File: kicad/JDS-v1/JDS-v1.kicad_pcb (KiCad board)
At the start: 2 copper layers, 2 parts, among them U1 74HC595

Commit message: finished diode board and initial seed board
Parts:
- added D1: 1N4148, Diode_THT:D_DO-35_SOD27_P7.62mm_Horizontal, F.Cu at (157.0, 54.2)
- added D10: 1N4148, Diode_THT:D_DO-35_SOD27_P7.62mm_Horizontal, F.Cu at (130.0, 54.0)
- added D11: 1N4148, Diode_THT:D_DO-35_SOD27_P7.62mm_Horizontal, F.Cu at (127.0, 54.0)
- added D12: 1N4148, Diode_THT:D_DO-35_SOD27_P7.62mm_Horizontal, F.Cu at (124.0, 54.0)
- added D13: 1N4148, Diode_THT:D_DO-35_SOD27_P7.62mm_Horizontal, F.Cu at (121.0, 54.0)
- added D14: 1N4148, Diode_THT:D_DO-35_SOD27_P7.62mm_Horizontal, F.Cu at (118.0, 54.0)
- added D15: 1N4148, Diode_THT:D_DO-35_SOD27_P7.62mm_Horizontal, F.Cu at (115.0, 54.0)
- added D16: 1N4148, Diode_THT:D_DO-35_SOD27_P7.62mm_Horizontal, F.Cu at (112.0, 54.0)
- added D17: 1N4148, Diode_THT:D_DO-35_SOD27_P7.62mm_Horizontal, F.Cu at (157.0, 68.0)
- added D18: 1N4148, Diode_THT:D_DO-35_SOD27_P7.62mm_Horizontal, F.Cu at (154.0, 68.0)
- added D19: 1N4148, Diode_THT:D_DO-35_SOD27_P7.62mm_Horizontal, F.Cu at (151.0, 68.0)
- added D2: 1N4148, Diode_THT:D_DO-35_SOD27_P7.62mm_Horizontal, F.Cu at (154.0, 54.2)
- added D20: 1N4148, Diode_THT:D_DO-35_SOD27_P7.62mm_Horizontal, F.Cu at (148.0, 68.0)
- added D21: 1N4148, Diode_THT:D_DO-35_SOD27_P7.62mm_Horizontal, F.Cu at (145.0, 68.0)
- added D22: 1N4148, Diode_THT:D_DO-35_SOD27_P7.62mm_Horizontal, F.Cu at (142.0, 68.0)
- added D23: 1N4148, Diode_THT:D_DO-35_SOD27_P7.62mm_Horizontal, F.Cu at (139.0, 68.0)
- added D24: 1N4148, Diode_THT:D_DO-35_SOD27_P7.62mm_Horizontal, F.Cu at (136.0, 68.0)
- added D25: 1N4148, Diode_THT:D_DO-35_SOD27_P7.62mm_Horizontal, F.Cu at (133.0, 68.0)
- added D26: 1N4148, Diode_THT:D_DO-35_SOD27_P7.62mm_Horizontal, F.Cu at (130.0, 68.0)
- added D27: 1N4148, Diode_THT:D_DO-35_SOD27_P7.62mm_Horizontal, F.Cu at (127.0, 68.0)
- added D28: 1N4148, Diode_THT:D_DO-35_SOD27_P7.62mm_Horizontal, F.Cu at (124.0, 68.0)
- added D29: 1N4148, Diode_THT:D_DO-35_SOD27_P7.62mm_Horizontal, F.Cu at (121.0, 68.0)
- added D3: 1N4148, Diode_THT:D_DO-35_SOD27_P7.62mm_Horizontal, F.Cu at (151.0, 54.2)
- added D30: 1N4148, Diode_THT:D_DO-35_SOD27_P7.62mm_Horizontal, F.Cu at (118.0, 68.0)
- added D31: 1N4148, Diode_THT:D_DO-35_SOD27_P7.62mm_Horizontal, F.Cu at (115.0, 68.0)
- added D32: 1N4148, Diode_THT:D_DO-35_SOD27_P7.62mm_Horizontal, F.Cu at (112.0, 68.0)
- added D33: 1N4148, Diode_THT:D_DO-35_SOD27_P7.62mm_Horizontal, F.Cu at (157.0, 82.2)
- added D34: 1N4148, Diode_THT:D_DO-35_SOD27_P7.62mm_Horizontal, F.Cu at (154.0, 82.2)
- added D35: 1N4148, Diode_THT:D_DO-35_SOD27_P7.62mm_Horizontal, F.Cu at (151.0, 82.2)
- added D36: 1N4148, Diode_THT:D_DO-35_SOD27_P7.62mm_Horizontal, F.Cu at (148.0, 82.2)
- added D37: 1N4148, Diode_THT:D_DO-35_SOD27_P7.62mm_Horizontal, F.Cu at (145.0, 82.2)
- added D38: 1N4148, Diode_THT:D_DO-35_SOD27_P7.62mm_Horizontal, F.Cu at (142.0, 82.2)
- added D39: 1N4148, Diode_THT:D_DO-35_SOD27_P7.62mm_Horizontal, F.Cu at (139.0, 82.2)
- added D4: 1N4148, Diode_THT:D_DO-35_SOD27_P7.62mm_Horizontal, F.Cu at (148.0, 54.2)
- added D40: 1N4148, Diode_THT:D_DO-35_SOD27_P7.62mm_Horizontal, F.Cu at (136.0, 82.2)
- added D41: 1N4148, Diode_THT:D_DO-35_SOD27_P7.62mm_Horizontal, F.Cu at (133.0, 82.0)
- added D42: 1N4148, Diode_THT:D_DO-35_SOD27_P7.62mm_Horizontal, F.Cu at (130.0, 82.0)
- added D43: 1N4148, Diode_THT:D_DO-35_SOD27_P7.62mm_Horizontal, F.Cu at (127.0, 82.0)
- added D44: 1N4148, Diode_THT:D_DO-35_SOD27_P7.62mm_Horizontal, F.Cu at (124.0, 82.0)
- added D45: 1N4148, Diode_THT:D_DO-35_SOD27_P7.62mm_Horizontal, F.Cu at (121.0, 82.0)
- added D46: 1N4148, Diode_THT:D_DO-35_SOD27_P7.62mm_Horizontal, F.Cu at (118.0, 82.0)
- added D47: 1N4148, Diode_THT:D_DO-35_SOD27_P7.62mm_Horizontal, F.Cu at (115.0, 82.0)
- added D48: 1N4148, Diode_THT:D_DO-35_SOD27_P7.62mm_Horizontal, F.Cu at (112.0, 82.0)
- added D49: 1N4148, Diode_THT:D_DO-35_SOD27_P7.62mm_Horizontal, F.Cu at (157.0, 96.0)
- added D5: 1N4148, Diode_THT:D_DO-35_SOD27_P7.62mm_Horizontal, F.Cu at (145.0, 54.2)
- added D50: 1N4148, Diode_THT:D_DO-35_SOD27_P7.62mm_Horizontal, F.Cu at (154.0, 96.0)
- added D51: 1N4148, Diode_THT:D_DO-35_SOD27_P7.62mm_Horizontal, F.Cu at (151.0, 96.0)
- added D52: 1N4148, Diode_THT:D_DO-35_SOD27_P7.62mm_Horizontal, F.Cu at (148.0, 96.0)
- added D53: 1N4148, Diode_THT:D_DO-35_SOD27_P7.62mm_Horizontal, F.Cu at (145.0, 96.0)
- added D54: 1N4148, Diode_THT:D_DO-35_SOD27_P7.62mm_Horizontal, F.Cu at (142.0, 96.0)
- added D55: 1N4148, Diode_THT:D_DO-35_SOD27_P7.62mm_Horizontal, F.Cu at (139.0, 96.0)
- added D56: 1N4148, Diode_THT:D_DO-35_SOD27_P7.62mm_Horizontal, F.Cu at (136.0, 96.0)
- added D57: 1N4148, Diode_THT:D_DO-35_SOD27_P7.62mm_Horizontal, F.Cu at (133.0, 96.0)
- added D58: 1N4148, Diode_THT:D_DO-35_SOD27_P7.62mm_Horizontal, F.Cu at (130.0, 96.0)
- added D59: 1N4148, Diode_THT:D_DO-35_SOD27_P7.62mm_Horizontal, F.Cu at (127.0, 96.0)
- added D6: 1N4148, Diode_THT:D_DO-35_SOD27_P7.62mm_Horizontal, F.Cu at (142.0, 54.2)
- added D60: 1N4148, Diode_THT:D_DO-35_SOD27_P7.62mm_Horizontal, F.Cu at (124.0, 96.0)
- added D61: 1N4148, Diode_THT:D_DO-35_SOD27_P7.62mm_Horizontal, F.Cu at (121.0, 96.0)
- added D62: 1N4148, Diode_THT:D_DO-35_SOD27_P7.62mm_Horizontal, F.Cu at (118.0, 96.0)
- added D63: 1N4148, Diode_THT:D_DO-35_SOD27_P7.62mm_Horizontal, F.Cu at (115.0, 96.0)
- added D64: 1N4148, Diode_THT:D_DO-35_SOD27_P7.62mm_Horizontal, F.Cu at (112.0, 96.0)
- added D7: 1N4148, Diode_THT:D_DO-35_SOD27_P7.62mm_Horizontal, F.Cu at (139.0, 54.2)
- added D8: 1N4148, Diode_THT:D_DO-35_SOD27_P7.62mm_Horizontal, F.Cu at (136.0, 54.2)
- added D9: 1N4148, Diode_THT:D_DO-35_SOD27_P7.62mm_Horizontal, F.Cu at (133.0, 54.0)
- added J1: toPegMatrix, Connector_PinHeader_2.54mm:PinHeader_1x08_P2.54mm_Vertical, F.Cu at (176.0, 53.0)
- added J10: mInJA, Connector_PinHeader_2.54mm:PinHeader_1x08_P2.54mm_Vertical, F.Cu at (162.0, 70.0)
- added J11: mInJB, Connector_PinHeader_2.54mm:PinHeader_1x08_P2.54mm_Vertical, F.Cu at (194.0, 72.0)
- added J2: fromPegsA, Connector_PinHeader_2.54mm:PinHeader_1x08_P2.54mm_Vertical, F.Cu at (155.0, 65.0)
- added J3: fromPegsB, Connector_PinHeader_2.54mm:PinHeader_1x08_P2.54mm_Vertical, F.Cu at (131.0, 65.0)
- added J4: fromPegsC, Connector_PinHeader_2.54mm:PinHeader_1x08_P2.54mm_Vertical, F.Cu at (154.5, 79.0)
- added J5: fromPegsD, Connector_PinHeader_2.54mm:PinHeader_1x08_P2.54mm_Vertical, F.Cu at (131.0, 79.0)
- added J6: fromPegsE, Connector_PinHeader_2.54mm:PinHeader_1x08_P2.54mm_Vertical, F.Cu at (156.0, 93.0)
- added J7: fromPegsF, Connector_PinHeader_2.54mm:PinHeader_1x08_P2.54mm_Vertical, F.Cu at (131.0, 93.0)
- added J8: fromPegsG, Connector_PinHeader_2.54mm:PinHeader_1x08_P2.54mm_Vertical, F.Cu at (155.0, 107.0)
- added J9: fromPegsH, Connector_PinHeader_2.54mm:PinHeader_1x08_P2.54mm_Vertical, F.Cu at (132.0, 107.0)
- moved A1 75.6 mm to (198.5, 54.0)
- moved U1 49.2 mm to (180.0, 55.5)
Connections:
- A1 pad 10: pm-in2 -> Net-(A1-Pad10)
- A1 pad 11: pm-in3 -> Net-(A1-Pad11)
- A1 pad 12: pm-in4 -> Net-(A1-Pad12)
- A1 pad 13: pm-in5 -> Net-(A1-Pad13)
- A1 pad 14: pm-in6 -> Net-(A1-Pad14)
- A1 pad 15: pm-in7 -> Net-(A1-Pad15)
- A1 pad 4: pm-clock -> pm-serial
- A1 pad 6: pm-serial -> pm-clock
- A1 pad 8: pm-in0 -> Net-(A1-Pad8)
- A1 pad 9: pm-in1 -> Net-(A1-Pad9)
- U1 pad 1: pm-out1 -> pm-out2
- U1 pad 15: pm-out0 -> pm-out1
- U1 pad 2: pm-out2 -> pm-out3
- U1 pad 3: pm-out3 -> pm-out4
- U1 pad 4: pm-out4 -> pm-out5
- U1 pad 5: pm-out5 -> pm-out6
- U1 pad 6: pm-out6 -> pm-out7
- U1 pad 7: pm-out7 -> pm-out8
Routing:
- net pm-in2: track 0.00 -> 64.0 mm
- net pm-in8: track 0.00 -> 59.7 mm
- net pm-in4: track 0.00 -> 55.8 mm
- net pm-in6: track 0.00 -> 53.4 mm
- net +3V3: track 0.00 -> 47.8 mm
- net pm-in1: track 0.00 -> 38.9 mm
- net pm-in7: track 0.00 -> 33.9 mm
- net pm-in3: track 0.00 -> 30.2 mm
- net pm-in5: track 0.00 -> 27.0 mm
- net GND: track 0.00 -> 15.9 mm
- net pm-out1: track 0.00 -> 14.4 mm
- net pm-enable: track 0.00 -> 11.5 mm, vias 0 -> 2
- net pm-clock: track 0.00 -> 11.4 mm, vias 0 -> 2
- net pm-serial: track 0.00 -> 11.4 mm, vias 0 -> 2
- net Net-(A1-Pad9): track 0.00 -> 4.59 mm
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- added copper zone on B.Cu, net GND

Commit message: iteration, and first print files
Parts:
- added J12: Out, NateTemp:StereoJackTRS3, F.Cu at (214.0, 64.0)
- moved J1 78.0 mm to (251.0, 74.5), turned to 270 degrees
- moved U1 72.3 mm to (248.5, 78.5), turned to 270 degrees
- moved A1 67.1 mm to (250.0, 97.0), turned to 270 degrees
- moved J11 43.2 mm to (232.0, 92.5), turned to 270 degrees
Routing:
- net toAmpR: track 0.00 -> 26.8 mm
- net toAmpL: track 0.00 -> 19.3 mm

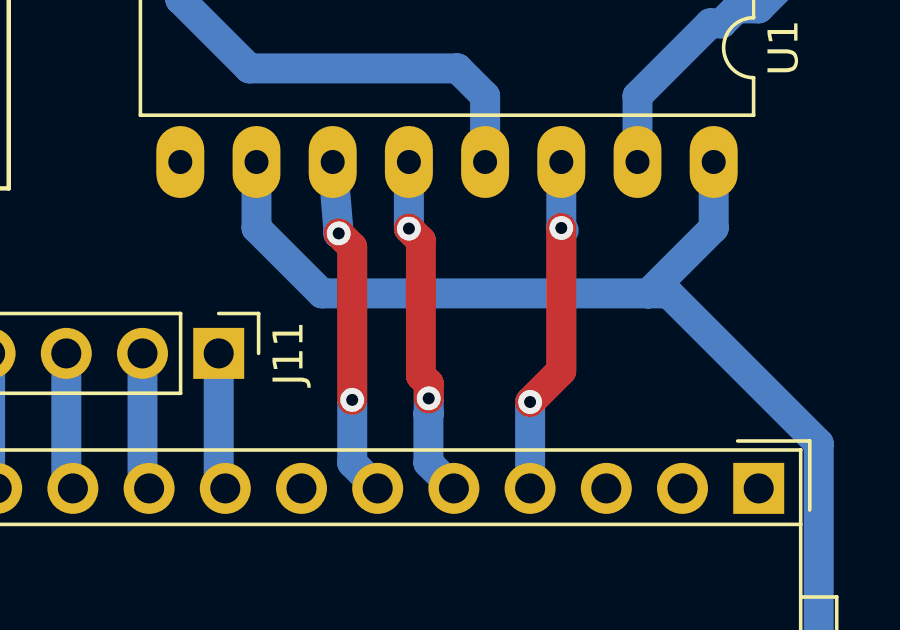
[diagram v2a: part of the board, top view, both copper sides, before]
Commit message: swapped 4 and 6 pins from seed to 595
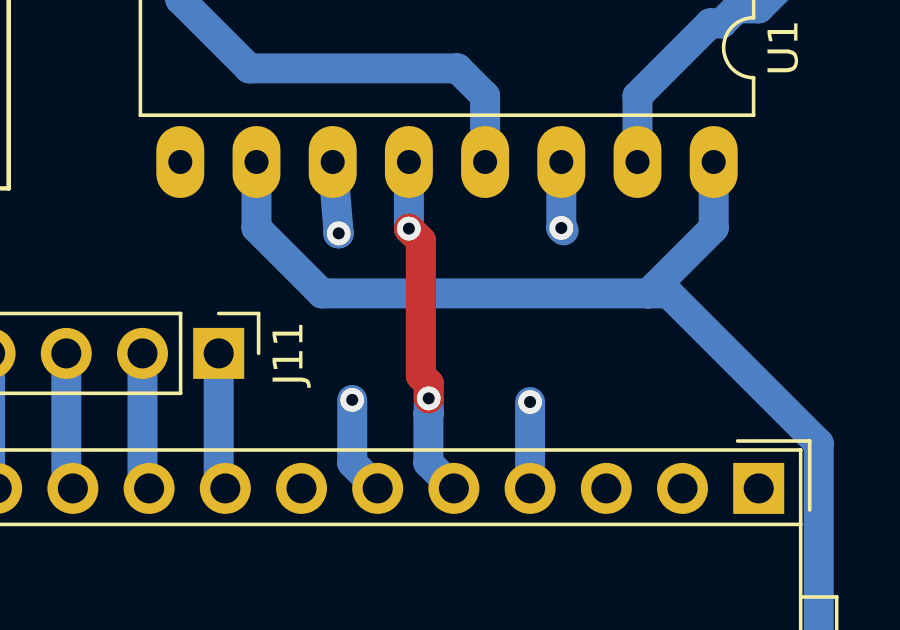
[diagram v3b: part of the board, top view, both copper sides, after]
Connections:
- A1 pad 4: pm-serial -> pm-clock
- A1 pad 6: pm-clock -> pm-serial
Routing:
- net pm-clock: track 11.4 -> 5.29 mm
- net pm-serial: track 11.4 -> 5.62 mm
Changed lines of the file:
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@@
-(kicad_pcb (version 20171130) (host pcbnew "(5.1.5-0)")
+(kicad_pcb (version 20171130) (host pcbnew "(5.0.0)")
   (general
     (thickness 1.6)
     (drawings 0)
-    (tracks 267)
+    (tracks 263)
     (zones 0)
     (modules 78)
@@
   )
   (setup
-    (last_trace_width 1)
+    (last_trace_width 0.25)
     (user_trace_width 0.5)
     (user_trace_width 1)
@@
     (zone_45_only no)
     (trace_min 0.2)
+    (segment_width 0.2)
+    (edge_width 0.05)
     (via_size 0.8)
     (via_drill 0.4)
@@
     (uvia_min_size 0.2)
     (uvia_min_drill 0.1)
-    (edge_width 0.05)
-    (segment_width 0.2)
     (pcb_text_width 0.3)
     (pcb_text_size 1.5 1.5)
@@
     (solder_mask_min_width 0.25)
     (aux_axis_origin 0 0)
-    (visible_elements FFFFFF7F)
+    (visible_elements 7FFFFFFF)
     (pcbplotparams
       (layerselection 0x010fc_ffffffff)
@@
       (net 44 "Net-(A1-Pad7)"))
     (pad 6 thru_hole circle (at 0 12.7 270) (size 1.7 1.7) (drill 1) (layers *.Cu *.Mask)
-      (net 9 pm-clock))
+      (net 4 pm-serial))
     (pad 5 thru_hole circle (at 0 10.16 270) (size 1.7 1.7) (drill 1) (layers *.Cu *.Mask)
       (net 7 pm-enable))
     (pad 4 thru_hole circle (at 0 7.62 270) (size 1.7 1.7) (drill 1) (layers *.Cu *.Mask)
-      (net 4 pm-serial))
+      (net 9 pm-clock))
     (pad 3 thru_hole circle (at 0 5.08 270) (size 1.7 1.7) (drill 1) (layers *.Cu *.Mask)
       (net 45 "Net-(A1-Pad3)"))
@@
   (segment (start 243.42 88.32) (end 243.42 88.32) (width 1) (layer B.Cu) (net 4))
   (via (at 243.42 88.32) (size 0.8) (drill 0.4) (layers F.Cu B.Cu) (net 4))
-  (segment (start 242.38 97) (end 242.38 94.12) (width 1) (layer B.Cu) (net 4))
-  (segment (start 242.38 94.12) (end 242.38 94.12) (width 1) (layer B.Cu) (net 4))
-  (via (at 242.38 94.12) (size 0.8) (drill 0.4) (layers F.Cu B.Cu) (net 4))
-  (segment (start 243.42 93.08) (end 242.38 94.12) (width 1) (layer F.Cu) (net 4))
-  (segment (start 243.42 88.32) (end 243.42 93.08) (width 1) (layer F.Cu) (net 4))
+  (segment (start 242.38 97) (end 242.38 94.12) (width 1) (layer B.Cu) (net 9))
+  (segment (start 242.38 94.12) (end 242.38 94.12) (width 1) (layer B.Cu) (net 9))
+  (via (at 242.38 94.12) (size 0.8) (drill 0.4) (layers F.Cu B.Cu) (net 9))
   (segment (start 238.3 78.46) (end 238.34 78.5) (width 1) (layer B.Cu) (net 5))
   (segment (start 238.3 74.5) (end 238.3 78.46) (width 1) (layer B.Cu) (net 5))
@@
   (segment (start 235.8 86.12) (end 236 88.5) (width 1) (layer B.Cu) (net 9))
   (segment (start 236 88.5) (end 236 88.5) (width 1) (layer B.Cu) (net 9))
-  (via (at 236 88.5) (size 0.8) (drill 0.4) (layers F.Cu B.Cu) (net 9) (status 1000000))
-  (segment (start 236.450001 96.150001) (end 236.450001 94.049999) (width 1) (layer B.Cu) (net 9))
-  (segment (start 237.3 97) (end 236.450001 96.150001) (width 1) (layer B.Cu) (net 9))
-  (segment (start 236.450001 94.049999) (end 236.450001 94.049999) (width 1) (layer B.Cu) (net 9))
-  (via (at 236.450001 94.049999) (size 0.8) (drill 0.4) (layers F.Cu B.Cu) (net 9))
-  (segment (start 236.450001 88.950001) (end 236 88.5) (width 1) (layer F.Cu) (net 9))
-  (segment (start 236.450001 94.049999) (end 236.450001 88.950001) (width 1) (layer F.Cu) (net 9))
+  (via (at 236 88.5) (size 0.8) (drill 0.4) (layers F.Cu B.Cu) (net 9))
+  (segment (start 236.450001 96.150001) (end 236.450001 94.049999) (width 1) (layer B.Cu) (net 4))
+  (segment (start 237.3 97) (end 236.450001 96.150001) (width 1) (layer B.Cu) (net 4))
+  (segment (start 236.450001 94.049999) (end 236.450001 94.049999) (width 1) (layer B.Cu) (net 4))
+  (via (at 236.450001 94.049999) (size 0.8) (drill 0.4) (layers F.Cu B.Cu) (net 4))
   (segment (start 245.92 78.46) (end 245.96 78.5) (width 1) (layer B.Cu) (net 10))
   (segment (start 245.92 74.5) (end 245.92 78.46) (width 1) (layer B.Cu) (net 10))

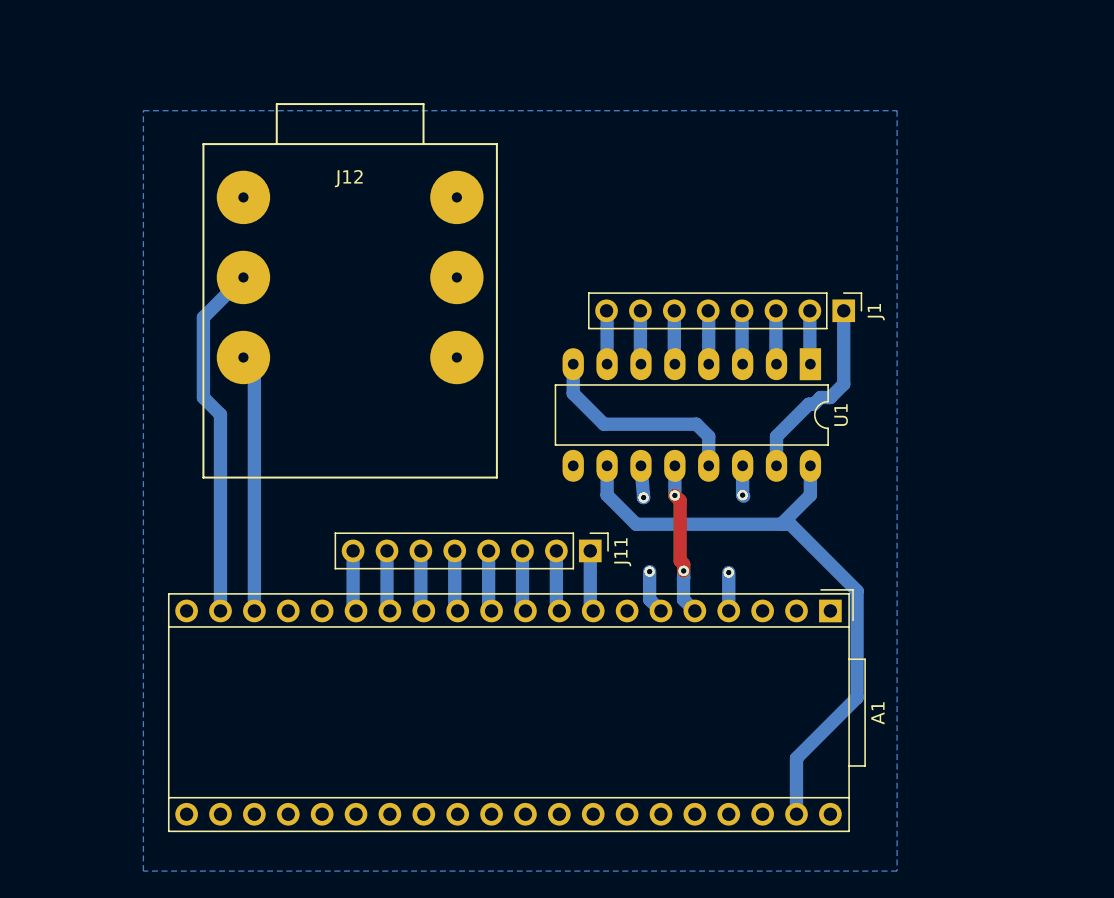
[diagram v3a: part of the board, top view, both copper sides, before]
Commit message: added output buffer and first 9v-5v-3.3v power supply
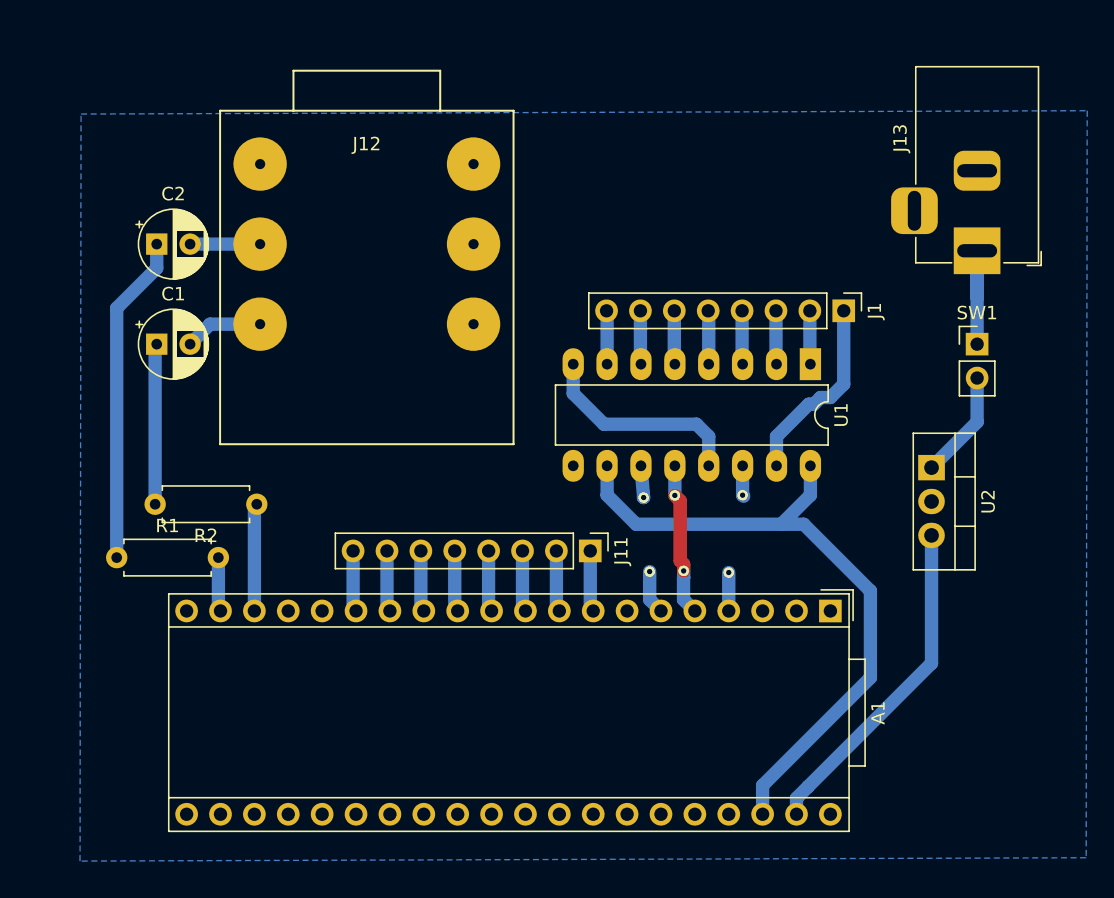
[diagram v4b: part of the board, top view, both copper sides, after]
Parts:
- added C1: 10uF, Capacitor_THT:CP_Radial_D5.0mm_P2.50mm, F.Cu at (199.5, 77.0)
- added C2: 10uF, Capacitor_THT:CP_Radial_D5.0mm_P2.50mm, F.Cu at (199.5, 69.5)
- added J13: Barrel_Jack_Switch, Connector_BarrelJack:BarrelJack_Horizontal, F.Cu at (261.0, 70.0)
- added R1: 100, Resistor_THT:R_Axial_DIN0207_L6.3mm_D2.5mm_P7.62mm_Horizontal, F.Cu at (196.5, 93.0)
- added R2: 100, Resistor_THT:R_Axial_DIN0207_L6.3mm_D2.5mm_P7.62mm_Horizontal, F.Cu at (207.0, 89.0)
- added SW1: POW-SW, Connector_PinHeader_2.54mm:PinHeader_1x02_P2.54mm_Vertical, F.Cu at (261.0, 77.0)
- added U2: LM7805_TO220, Package_TO_SOT_THT:TO-220-3_Vertical, F.Cu at (257.6, 86.3)
- moved J12 2.80 mm to (215.2, 61.5)
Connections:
- A1 pad 38: Net-(A1-Pad38) -> +3V3
- A1 pad 39: +3V3 -> +5V
- J12 pad 3: toAmpR -> Net-(C2-Pad2)
- J12 pad 5: toAmpL -> Net-(C1-Pad2)
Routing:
- net +5V: track 0.00 -> 25.3 mm
- net Net-(C2-Pad1): track 0.00 -> 24.7 mm
- net toAmpR: track 26.8 -> 4.07 mm
- net Net-(C1-Pad1): track 0.00 -> 12.0 mm
- net toAmpL: track 19.3 -> 8.07 mm
- net Net-(J13-Pad1): track 0.00 -> 10.0 mm
- net Net-(SW1-Pad2): track 0.00 -> 8.33 mm
- net Net-(C1-Pad2): track 0.00 -> 5.87 mm
- net Net-(C2-Pad2): track 0.00 -> 5.25 mm
- net +3V3: track 47.8 -> 50.3 mm
